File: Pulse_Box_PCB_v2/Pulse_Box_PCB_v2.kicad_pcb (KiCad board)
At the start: 2 copper layers, 80 x 59 mm, 60 parts, among them J1 Screw_Terminal_01x02, J2 Conn_01x11, J3 Conn_01x11, J4 Conn_01x03, J5 Conn_01x03, J6 Conn_01x03_Pin, J7 Conn_01x04, P1 USB_C_Plug_USB2.0, SW1 SW_Push, SW2 SW_Push, U1 ESP32-S3-WROOM-1, U2 USBLC6-2SC6, U3 TPS54560BDDA, U4 SN74LV1T34DBV, U5 74LVC1G3157, U6 SN74LV1T34DBV, U8 AP2114-3.3TRG1

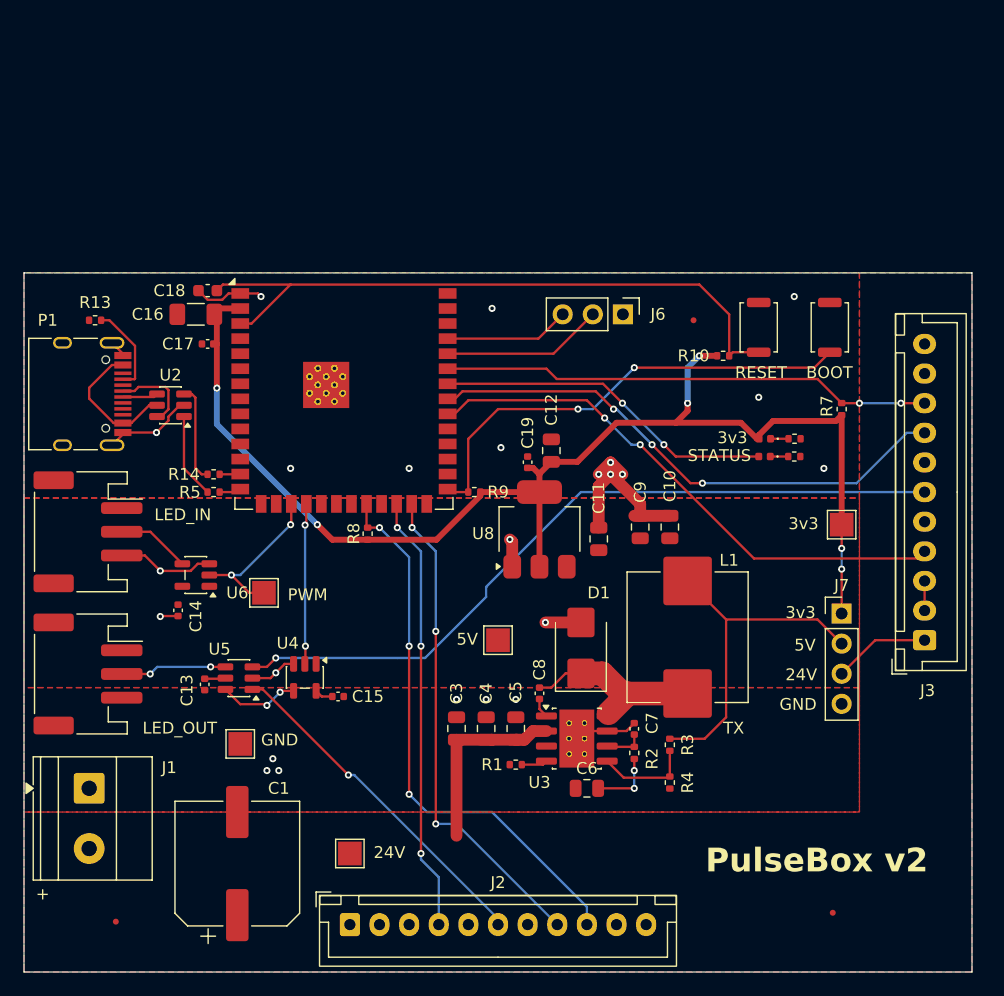
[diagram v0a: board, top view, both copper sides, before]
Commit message: complete v2 and v1 panel design, this is the final design sent to jlcpcb for v2
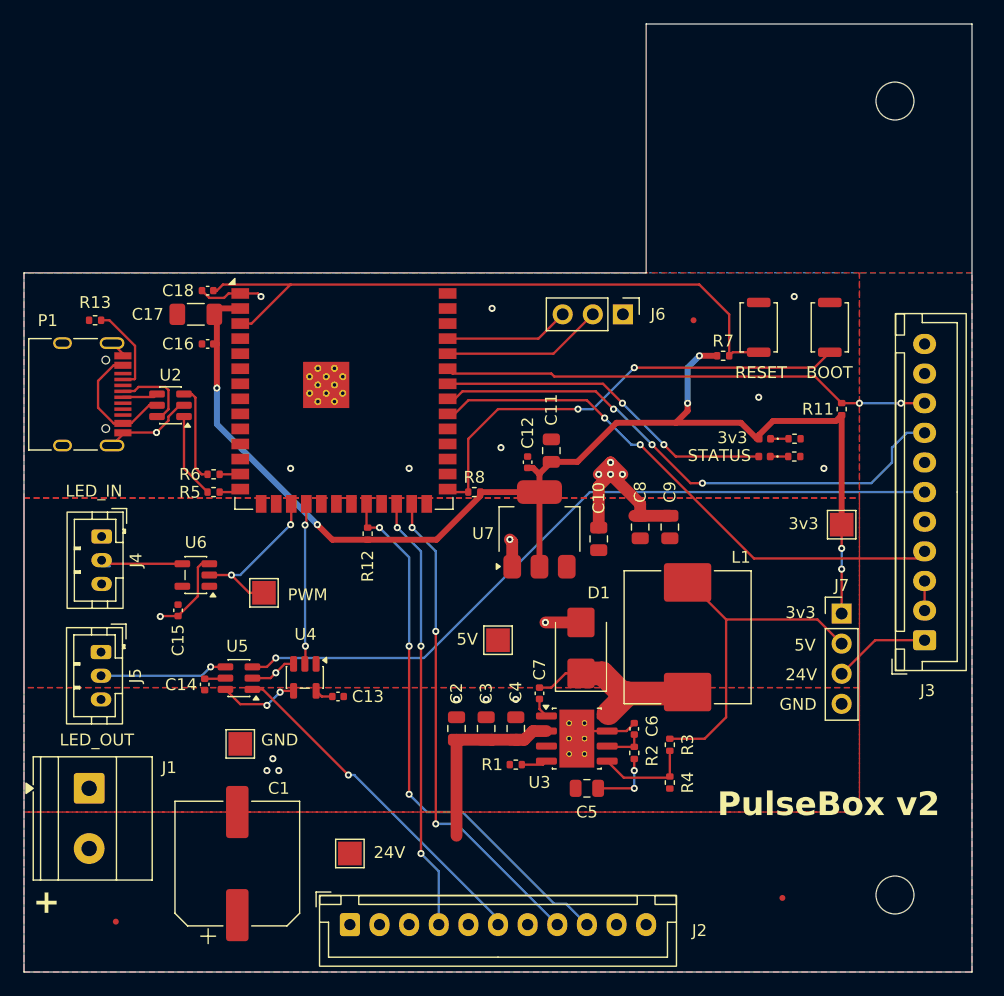
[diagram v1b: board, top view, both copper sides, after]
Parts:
- added H1: MountingHole, MountingHole:MountingHole_3.2mm_M3, F.Cu at (223.5, 36.5)
- added H2: MountingHole, MountingHole:MountingHole_3.2mm_M3, F.Cu at (223.5, 103.5)
- C18: footprint Capacitor_SMD:C_0603_1608Metric -> Capacitor_SMD:C_0402_1005Metric
- J4, J5: footprint Connector_JST:JST_PH_S3B-PH-SM4-TB_1x03-1MP_P2.00mm_Horizontal -> Connector_JST:JST_PH_B3B-PH-K_1x03_P2.00mm_Vertical
- L1: footprint Inductor_SMD:L_APV_APH1030 -> Inductor_SMD:L_TechFuse_SL1040
- moved FID2 4.43 mm to (214.0, 103.8)
- moved J5 2.15 mm to (156.5, 83.0)
- moved J4 1.22 mm to (156.6, 73.2)
- renumbered C11 to C10, C12 to C11, C19 to C12, C15 to C13, C13 to C14, C14 to C15, C17 to C16, C16 to C17, C3 to C2, C4 to C3, C5 to C4, C6 to C5, C7 to C6, C8 to C7, C9 to C8, C10 to C9, R12 to R10, R7 to R11, R8 to R12, R14 to R6, R10 to R7, R9 to R8, R11 to R9, U8 to U7
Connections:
- net PWM_OUT_S renamed PWM_OUT_N
- net S_SENS renamed N_SENS
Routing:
- net GND: track 58.3 -> 55.6 mm, vias 24 -> 23
- net PWM_DOUT: track 9.00 -> 10.8 mm, vias 2 -> 1
- net PWM_5V: track 6.23 -> 7.64 mm
- net N_SENS: track 47.0 -> 46.1 mm
- net UART1_RX: track 45.5 -> 46.2 mm
- net Net-(U2-VBUS): track 11.8 -> 11.0 mm
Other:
- board size 80 x 59 mm -> 80 x 80 mm
- board text removed: "TX"
